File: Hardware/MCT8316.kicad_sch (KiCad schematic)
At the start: 30 parts, among them J12 Screw_Terminal_01x04, J5 Screw_Terminal_01x03, J6 Screw_Terminal_01x03, J7 Conn_01x03_Pin, J8 Conn_01x03_Pin, U10 MCT8316, U12 ISO7721DR, U13 EL817, U14 EL817, U15 EL817

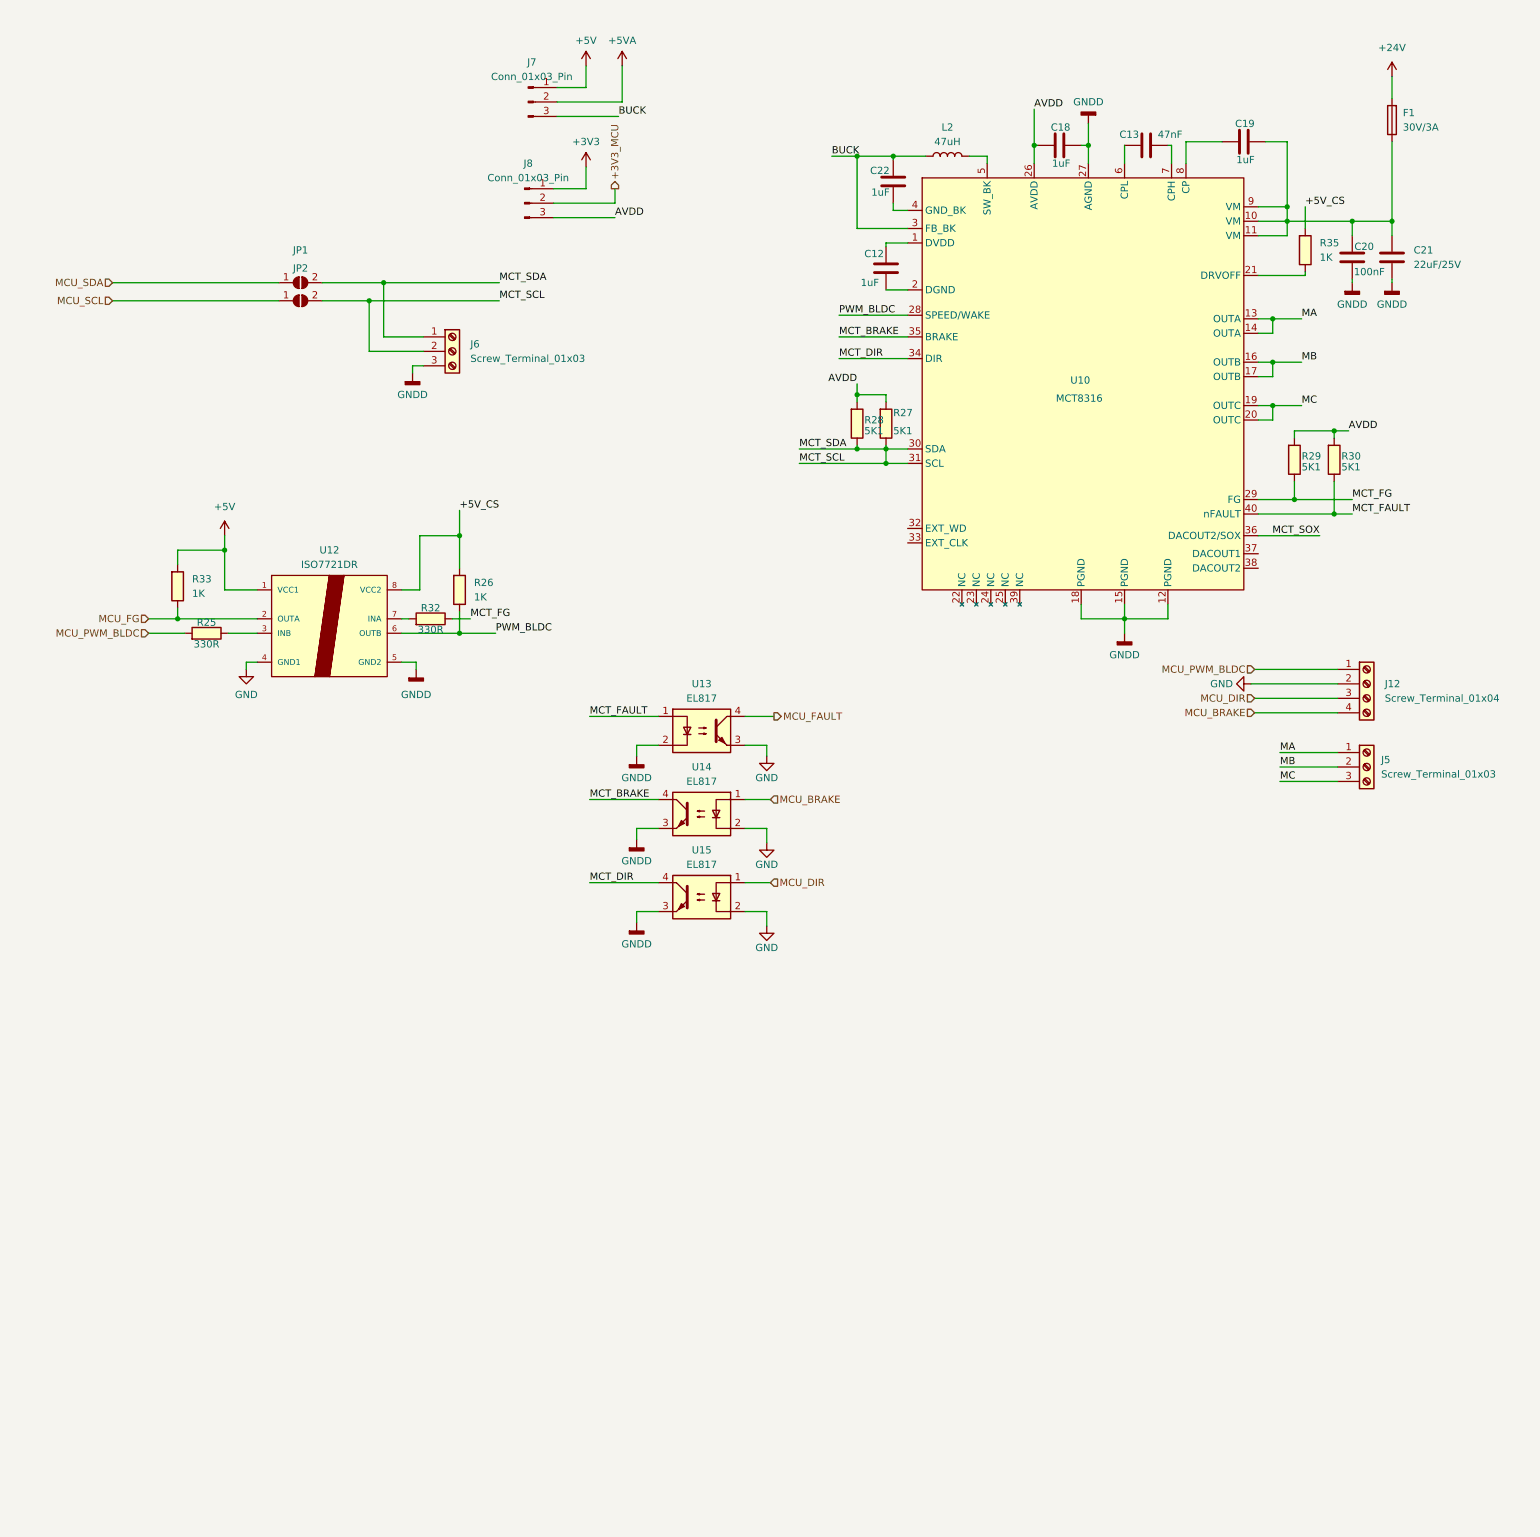
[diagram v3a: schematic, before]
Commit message: Update schematic part2
Vẽ bus dành cho khối BLDC
Đóng khối chức năng cho sheet MCT8316
Tạo sheet nguồn cho các mạch nguồn Buck DCDC, LDO LD1117, BS0505
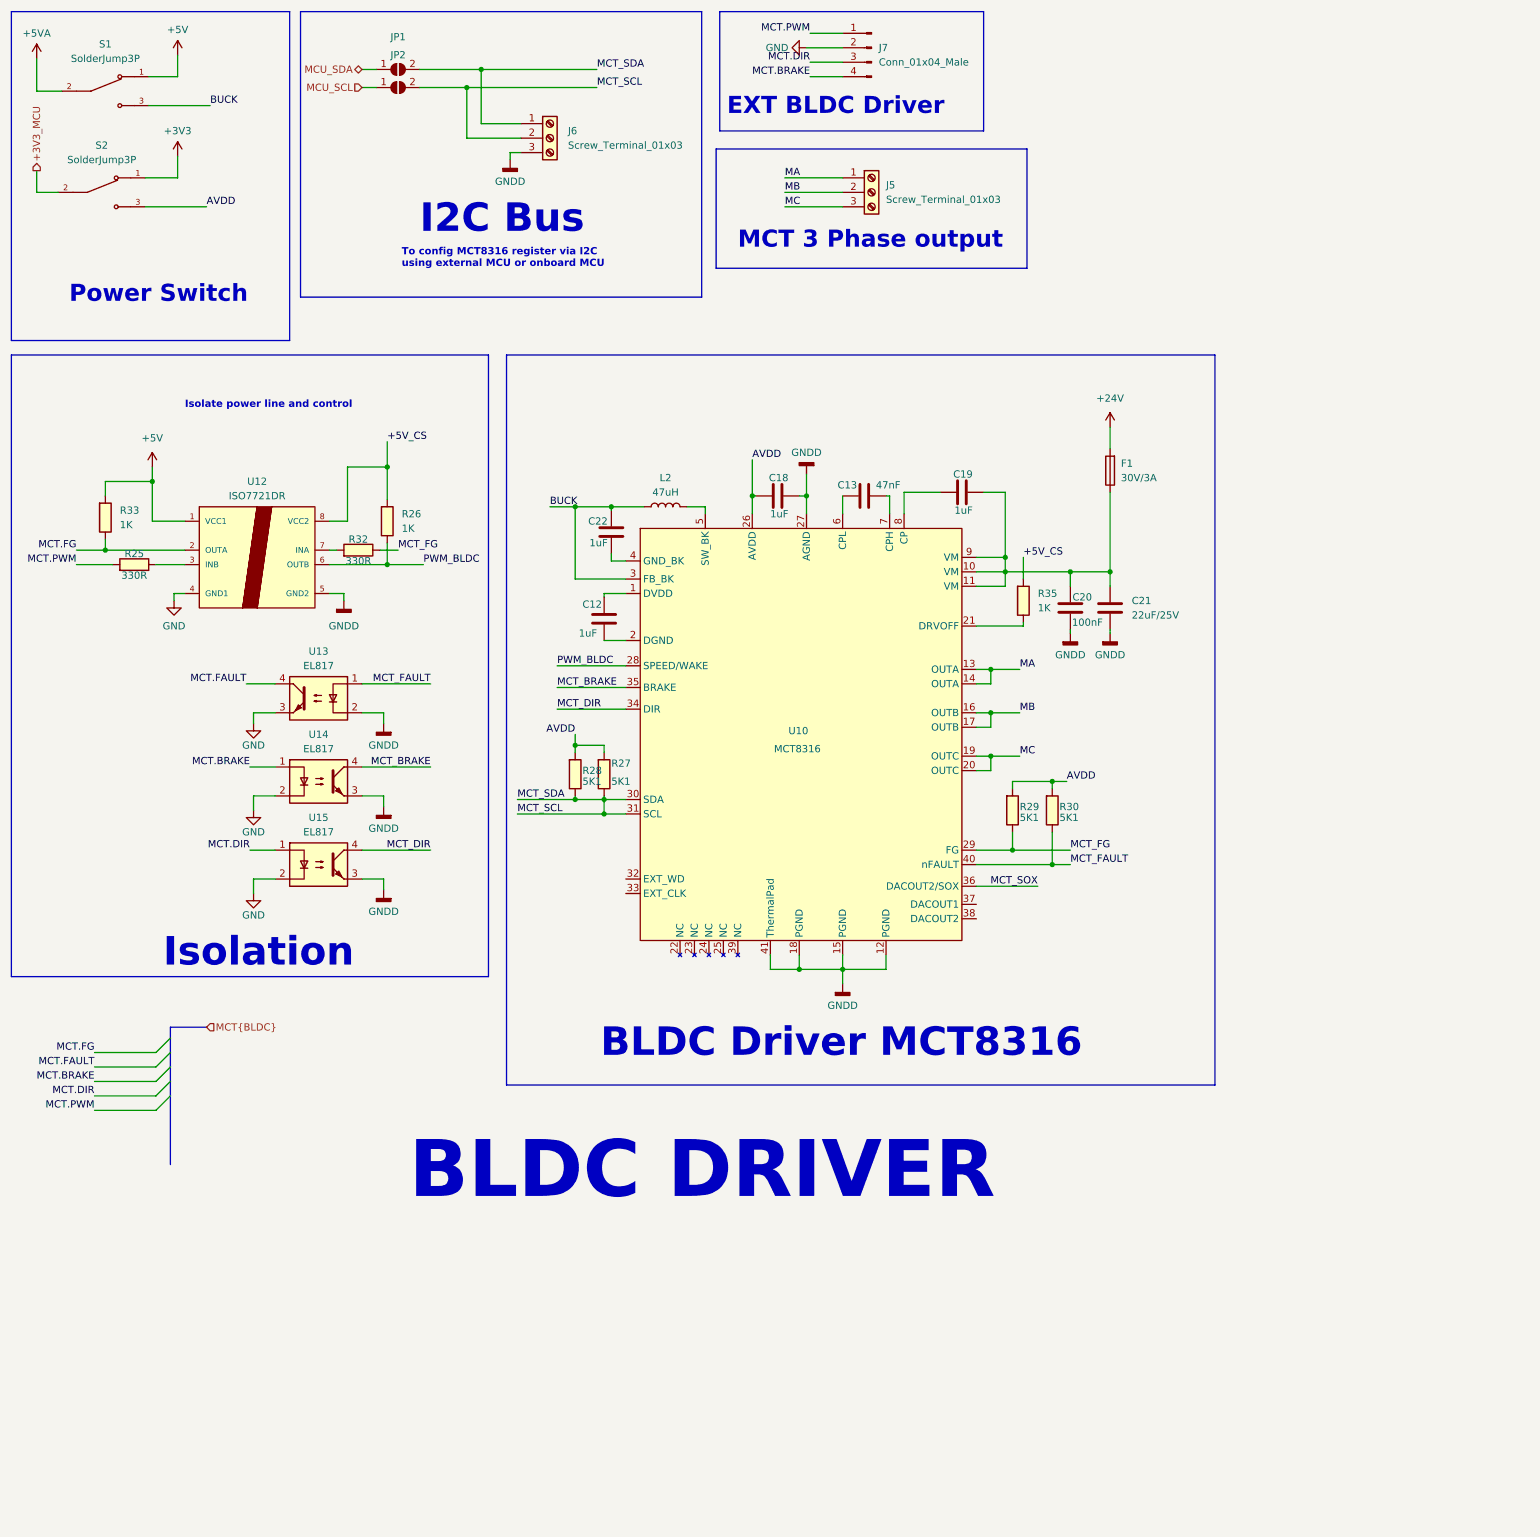
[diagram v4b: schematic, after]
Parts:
- removed J12: Screw_Terminal_01x04, Connector_PinHeader_2.54mm:PinHeader_1x04_P2.54mm_Vertical, symbol Connector:Screw_Terminal_01x04
- removed J7, J8: Conn_01x03_Pin, Connector_PinHeader_2.54mm:PinHeader_1x03_P2.54mm_Vertical, symbol IVS_SYMBOLS:Conn_01x03_Pin
- added J7: Conn_01x04_Male, IVS_FOOTPRINTS:Conn-Vert-THT-4P-2.54mm-S4B_XH_SM4_TB, symbol IVS_SYMBOLS:Conn_01x04_Male
- added S1, S2: SolderJump3P, Jumper:SolderJumper-3_P1.3mm_Open_RoundedPad1.0x1.5mm_NumberLabels, symbol IVS_SYMBOLS:EG1206
- J6: footprint Connector_PinHeader_2.54mm:PinHeader_1x03_P2.54mm_Vertical -> IVS_FOOTPRINTS:Conn-Horz-SMD-3P-2.54mm-S3B_XH_SM4_TB
- U12: footprint IVS_FOOTPRINTS:SOIC-8 -> IVS_FOOTPRINTS:SOIC-8_5.23x5.23mm_P1.27mm
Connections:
- net +3V3: now also S2.1
- net +3V3_MCU: now also S2.2
- net +5V: now also S1.1
- net +5VA: now also S1.2
- net AVDD: now also S2.3
- net BUCK: now also S1.3
- net GND: now also J7.2 (Pin_2)
- net GNDD: now also U10.41 (ThermalPad)
- net MCU_BRAKE renamed MCT.BRAKE
- net MCT.BRAKE: now also J7.4 (Pin_4)
- net MCU_DIR renamed MCT.DIR
- net MCT.DIR: now also J7.3 (Pin_3)
- net MCU_FAULT renamed MCT.FAULT
- net MCU_FG renamed MCT.FG
- net MCU_PWM_BLDC renamed MCT.PWM
- net MCT.PWM: now also J7.1 (Pin_1)
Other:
- note added: "BLDC DRIVER"
- note added: "BLDC Driver MCT8316"
- note added: "EXT BLDC Driver"
- note added: "I2C Bus"
- note added: "Isolate power line and control"
- note added: "Isolation"
- note added: "MCT 3 Phase output"
- note added: "Power Switch"
- note added: "To config MCT8316 register via I2C using external MCU or onboard MCU"
- moved on the sheet: C12, C13, C18, C19, C20, C21, C22, F1, J5, J6, JP1, JP2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

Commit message: Add PCB
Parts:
- J6: symbol Connector:Screw_Terminal_01x03 -> IVS_SYMBOLS:Conn_JST_SMD_3P
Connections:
- net GNDD: now also J6.S
- net MCT_SCL: no longer J6.1 (Pin_1), JP1.2 (B), R28.2, U10.30 (SDA)
- new net MCT_SDA: J6.1, JP1.2 (B), R28.2, U10.30 (SDA)
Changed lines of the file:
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@@
   (junction (at 34.925 111.125) (diameter 0) (color 0 0 0 0)
   )
-  (junction (at 122.555 154.94) (diameter 0) (color 0 0 0 0)
-  )
   (junction (at 194.31 163.83) (diameter 0) (color 0 0 0 0)
   )
@@
   (junction (at 100.965 26.67) (diameter 0) (color 0 0 0 0)
   )
+  (junction (at 113.03 45.72) (diameter 0) (color 0 0 0 0)
+  )
   (junction (at 98.425 29.845) (diameter 0) (color 0 0 0 0)
   )
@@
     (stroke (width 0) (type default))
   )
+  (wire (pts (xy 113.03 45.72) (xy 113.03 45.085))
+    (stroke (width 0) (type default))
+  )
   (wire (pts (xy 201.295 151.765) (xy 203.835 151.765))
     (stroke (width 0) (type default))
@@
     (stroke (width 0) (type default))
   )
-  (wire (pts (xy 117.475 154.94) (xy 122.555 154.94))
-    (stroke (width 0) (type default))
-  )
   (wire (pts (xy 92.075 163.83) (xy 80.01 163.83))
     (stroke (width 0) (type default))
@@
     (stroke (width 0) (type default))
   )
-  (wire (pts (xy 122.555 154.305) (xy 122.555 154.94))
+  (wire (pts (xy 122.555 154.305) (xy 122.555 157.48))
     (stroke (width 0) (type default))
   )
@@
     (stroke (width 0) (type default))
   )
+  (wire (pts (xy 106.045 45.72) (xy 113.03 45.72))
+    (stroke (width 0) (type default))
+  )
   (wire (pts (xy 22.86 44.45) (xy 22.86 48.26))
     (stroke (width 0) (type default))
@@
     (stroke (width 0) (type default))
   )
-  (wire (pts (xy 106.045 41.275) (xy 106.045 42.545))
-    (stroke (width 0) (type default))
-  )
   (wire (pts (xy 86.36 111.125) (xy 83.185 111.125))
     (stroke (width 0) (type default))
@@
     (stroke (width 0) (type default))
   )
+  (wire (pts (xy 106.045 41.275) (xy 106.045 45.72))
+    (stroke (width 0) (type default))
+  )
   (wire (pts (xy 64.77 149.225) (xy 60.325 149.225))
     (stroke (width 0) (type default))
@@
     (stroke (width 0) (type default))
   )
+  (wire (pts (xy 113.03 45.72) (xy 113.03 46.99))
+    (stroke (width 0) (type default))
+  )
   (wire (pts (xy 164.465 182.245) (xy 164.465 184.785))
     (stroke (width 0) (type default))
@@
     (stroke (width 0) (type default))
   )
-  (wire (pts (xy 122.555 154.94) (xy 122.555 157.48))
-    (stroke (width 0) (type default))
-  )
-  (wire (pts (xy 122.555 154.94) (xy 126.365 154.94))
+  (wire (pts (xy 117.475 154.94) (xy 126.365 154.94))
     (stroke (width 0) (type default))
   )
@@
     )
   )
-  (symbol (lib_id "power:GNDD") (at 106.045 42.545 0) (unit 1)
+  (symbol (lib_id "power:GNDD") (at 113.03 46.99 0) (unit 1)
     (in_bom yes) (on_board yes) (dnp no) (fields_autoplaced)
-    (property "Reference" "#PWR06" (at 106.045 48.895 0)
-      (effects (font (size 1.27 1.27)) hide)
-    )
-    (property "Value" "GNDD" (at 106.045 46.355 0)
-      (effects (font (size 1.27 1.27)))
-    )
-    (property "Footprint" "" (at 106.045 42.545 0)
-      (effects (font (size 1.27 1.27)) hide)
-    )
-    (property "Datasheet" "" (at 106.045 42.545 0)
+    (property "Reference" "#PWR06" (at 113.03 53.34 0)
+      (effects (font (size 1.27 1.27)) hide)
+    )
+    (property "Value" "GNDD" (at 113.03 50.8 0)
+      (effects (font (size 1.27 1.27)))
+    )
+    (property "Footprint" "" (at 113.03 46.99 0)
+      (effects (font (size 1.27 1.27)) hide)
+    )
+    (property "Datasheet" "" (at 113.03 46.99 0)
       (effects (font (size 1.27 1.27)) hide)
     )
@@
     )
   )
-  (symbol (lib_id "Connector:Screw_Terminal_01x03") (at 113.03 38.735 0) (unit 1)
+  (symbol (lib_id "IVS_SYMBOLS:Conn_JST_SMD_3P") (at 113.03 38.735 0) (unit 1)
     (in_bom yes) (on_board yes) (dnp no) (fields_autoplaced)
     (property "Reference" "J6" (at 116.205 37.465 0)
@@
       (effects (font (size 1.27 1.27)) (justify left))
     )
-    (property "Footprint" "IVS_FOOTPRINTS:Conn-Horz-SMD-3P-2.54mm-S3B_XH_SM4_TB" (at 113.03 38.735 0)
-      (effects (font (size 1.27 1.27)) hide)
-    )
-    (property "Datasheet" "~" (at 113.03 38.735 0)
+    (property "Footprint" "IVS_FOOTPRINTS:Conn-Horz-SMD-3P-2.54mm-S3B_XH_SM4_TB" (at 113.03 50.8 0)
+      (effects (font (size 1.27 1.27)) hide)
+    )
+    (property "Datasheet" "~" (at 111.125 46.99 0)
       (effects (font (size 1.27 1.27)) hide)
     )
@@
     (pin "2")
     (pin "3")
-    (instances
-      (project "DriverMotor"
+    (pin "S")
+    (instances
+      (project "DriverMotor"

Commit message: Layout PCB
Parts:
- J5: footprint TerminalBlock:TerminalBlock_bornier-3_P5.08mm -> IVS_FOOTPRINTS:TerminalBlock_bornier-3_P5.08mm
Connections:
- net MCU_SCL renamed MCT.SCL
- net MCU_SDA renamed MCT.SDA
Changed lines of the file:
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@@
+    (stroke (width 0) (type default))
+  )
+  (bus_entry (at 210.82 25.4) (size 2.54 -2.54)
+    (stroke (width 0) (type default))
+  )
+  (bus_entry (at 210.82 22.86) (size 2.54 -2.54)
     (stroke (width 0) (type default))
   )
@@
     (stroke (width 0) (type default))
   )
+  (bus (pts (xy 213.36 20.32) (xy 213.36 22.86))
+    (stroke (width 0) (type default))
+  )
   (wire (pts (xy 196.215 124.46) (xy 196.215 123.825))
     (stroke (width 0) (type default))
@@
     (stroke (width 0) (type default))
   )
+  (bus (pts (xy 213.36 22.86) (xy 213.36 37.465))
+    (stroke (width 0) (type default))
+  )
   (wire (pts (xy 92.075 163.83) (xy 80.01 163.83))
     (stroke (width 0) (type default))
@@
     (stroke (width 0) (type default))
   )
+  (wire (pts (xy 203.2 25.4) (xy 210.82 25.4))
+    (stroke (width 0) (type default))
+  )
   (wire (pts (xy 84.455 109.855) (xy 84.455 113.665))
     (stroke (width 0) (type default))
@@
     (stroke (width 0) (type default))
   )
+  (bus (pts (xy 219.075 17.78) (xy 213.36 17.78))
+    (stroke (width 0) (type default))
+  )
   (bus (pts (xy 46.355 201.93) (xy 46.355 204.47))
     (stroke (width 0) (type default))
@@
     (stroke (width 0) (type default))
   )
+  (wire (pts (xy 203.2 22.86) (xy 210.82 22.86))
+    (stroke (width 0) (type default))
+  )
   (wire (pts (xy 34.925 101.6) (xy 34.925 99.06))
     (stroke (width 0) (type default))
@@
     (stroke (width 0) (type default))
   )
-  (wire (pts (xy 196.215 112.395) (xy 196.215 116.205))
+  (wire (pts (xy 196.215 111.125) (xy 196.215 116.205))
     (stroke (width 0) (type default))
   )
@@
   )
   (wire (pts (xy 187.96 134.62) (xy 190.5 134.62))
+    (stroke (width 0) (type default))
+  )
+  (bus (pts (xy 213.36 17.78) (xy 213.36 20.32))
     (stroke (width 0) (type default))
   )
@@
     (effects (font (size 10 10) (thickness 2) bold) (justify left bottom))
   )
-  (text "I2C Bus" (at 90.17 55.88 0)
+  (text "I2C Bus" (at 88.9 59.69 0)
     (effects (font (size 5 5) bold) (justify left bottom))
   )
@@
   )
   (text "To config MCT8316 register via I2C \nusing external MCU or onboard MCU"
-    (at 86.995 61.595 0)
+    (at 85.725 65.405 0)
     (effects (font (size 1.27 1.27) bold) (justify left bottom))
   )
@@
     (effects (font (size 5 5) (thickness 2) bold) (justify left bottom))
   )
+  (label "MCT.SDA" (at 203.2 25.4 180) (fields_autoplaced)
+    (effects (font (size 1.27 1.27)) (justify right bottom))
+  )
+  (label "MCT.SCL" (at 80.01 29.845 180) (fields_autoplaced)
+    (effects (font (size 1.27 1.27)) (justify right bottom))
+  )
   (label "AVDD" (at 203.835 151.765 0) (fields_autoplaced)
     (effects (font (size 1.27 1.27)) (justify left bottom))
@@
     (effects (font (size 1.27 1.27)) (justify right bottom))
   )
-  (label "+5V_CS" (at 196.215 112.395 0) (fields_autoplaced)
-    (effects (font (size 1.27 1.27)) (justify left bottom))
-  )
   (label "MCT_BRAKE" (at 114.3 135.255 0) (fields_autoplaced)
     (effects (font (size 1.27 1.27)) (justify left bottom))
@@
     (effects (font (size 1.27 1.27)) (justify right bottom))
   )
+  (label "MCT.SDA" (at 80.01 26.67 180) (fields_autoplaced)
+    (effects (font (size 1.27 1.27)) (justify right bottom))
+  )
   (label "BUCK" (at 113.03 103.505 0) (fields_autoplaced)
     (effects (font (size 1.27 1.27)) (justify left bottom))
@@
     (effects (font (size 1.27 1.27)) (justify right bottom))
   )
-  (label "+5V_CS" (at 84.455 92.075 0) (fields_autoplaced)
-    (effects (font (size 1.27 1.27)) (justify left bottom))
-  )
   (label "MA" (at 195.58 132.08 0) (fields_autoplaced)
     (effects (font (size 1.27 1.27)) (justify left bottom))
@@
     (effects (font (size 1.27 1.27)) (justify left bottom))
   )
-  (hierarchical_label "MCU_SCL" (shape input) (at 80.01 29.845 180) (fields_autoplaced)
-    (effects (font (size 1.27 1.27)) (justify right))
+  (label "MCT.SCL" (at 203.2 22.86 180) (fields_autoplaced)
+    (effects (font (size 1.27 1.27)) (justify right bottom))
+  )
+  (hierarchical_label "+5V_CS" (shape input) (at 84.455 92.075 0) (fields_autoplaced)
+    (effects (font (size 1.27 1.27)) (justify left))
   )
   (hierarchical_label "MCT{BLDC}" (shape input) (at 52.705 194.945 0) (fields_autoplaced)
     (effects (font (size 1.27 1.27)) (justify left))
   )
-  (hierarchical_label "MCU_SDA" (shape bidirectional) (at 80.01 26.67 180) (fields_autoplaced)
-    (effects (font (size 1.27 1.27)) (justify right))
+  (hierarchical_label "MCT{I2C}" (shape bidirectional) (at 219.075 17.78 0) (fields_autoplaced)
+    (effects (font (size 1.27 1.27)) (justify left))
   )
   (hierarchical_label "+3V3_MCU" (shape output) (at 22.86 44.45 90) (fields_autoplaced)
+    (effects (font (size 1.27 1.27)) (justify left))
+  )
+  (hierarchical_label "+5V_CS" (shape input) (at 196.215 111.125 0) (fields_autoplaced)
     (effects (font (size 1.27 1.27)) (justify left))
   )
@@
   )
   (symbol (lib_id "power:GNDD") (at 113.03 46.99 0) (unit 1)
-    (in_bom yes) (on_board yes) (dnp no) (fields_autoplaced)
+    (in_bom yes) (on_board yes) (dnp no)
     (property "Reference" "#PWR06" (at 113.03 53.34 0)
       (effects (font (size 1.27 1.27)) hide)
@@
       (effects (font (size 1.27 1.27)) (justify left))
     )
-    (property "Footprint" "TerminalBlock:TerminalBlock_bornier-3_P5.08mm" (at 169.545 48.26 0)
-      (effects (font (size 1.27 1.27)) hide)
-    )
+    (property "Footprint" "IVS_FOOTPRINTS:TerminalBlock_bornier-3_P5.08mm" (at 169.545 48.26 0)
+      (effects (font (size 1.27 1.27)) hide)
+    )

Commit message: Update components
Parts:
- removed U13, U14, U15: EL817, IVS_FOOTPRINTS:OptoIsolation-EL357N-G, symbol IVS_SYMBOLS:EL817
- added C12: 10uF, IVS_FOOTPRINTS:C_0603, symbol Thu_vien_kicad:C
- added J8: Conn_01x03_Pin, IVS_FOOTPRINTS:Conn-Vert-THT-3P-2.54mm-S3B_XH_SM4_TB, symbol IVS_SYMBOLS:Conn_01x03_Pin
- added R14 (x2): 1K, IVS_FOOTPRINTS:R_0603, symbol Thu_vien_kicad:R
- added U18: ~, IVS_FOOTPRINTS:SOIC-16W_5.3x10.2mm_P1.27mm, symbol IVS_SYMBOLS:PS2801-4
- C21: footprint IVS_FOOTPRINTS:CP-Tantalum-EIA-3528-15-AVX-H -> Capacitor_Tantalum_SMD:CP_EIA-7343-15_Kemet-W_Pad2.25x2.55mm_HandSolder; symbol IVS_SYMBOLS:C -> IVS_SYMBOLS:C_Polarized
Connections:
- net +3V3_MCU: now also U18.7
- net GND: now also R14.2, U18.11, U18.2, U18.4
- net GNDD: now also U18.13, U18.15, U18.6, U18.9
- net MCT.BRAKE: now also U18.1
- net MCT.DIR: now also U18.3
- net MCT.FAULT: now also U18.12
- net MCT_BRAKE: now also U18.16
- net MCT_DIR: now also U18.14
- net MCT_FAULT: now also U18.5
- new net: C12.1, J8.2 (Pin_2)
- new net: J8.3 (Pin_3), R14.1
- new net: R14.1, U18.8
- new net: R14.2, U18.10
- new net +24V_CS: C12.2, J8.1 (Pin_1)
